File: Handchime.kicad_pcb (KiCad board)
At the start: 4 copper layers, 40.6 x 20.2 mm, 23 parts, among them J1 USB_C_Receptacle_USB2.0_16P, J2 Pins, J3 SWD, SW0 BOOT, SW1 Row 0, Col 0, SW2 Row 0, Col 1, U1 STM32C071GBUx, U2 PRTR5V0U2X, U3 XC6206P332MR-G

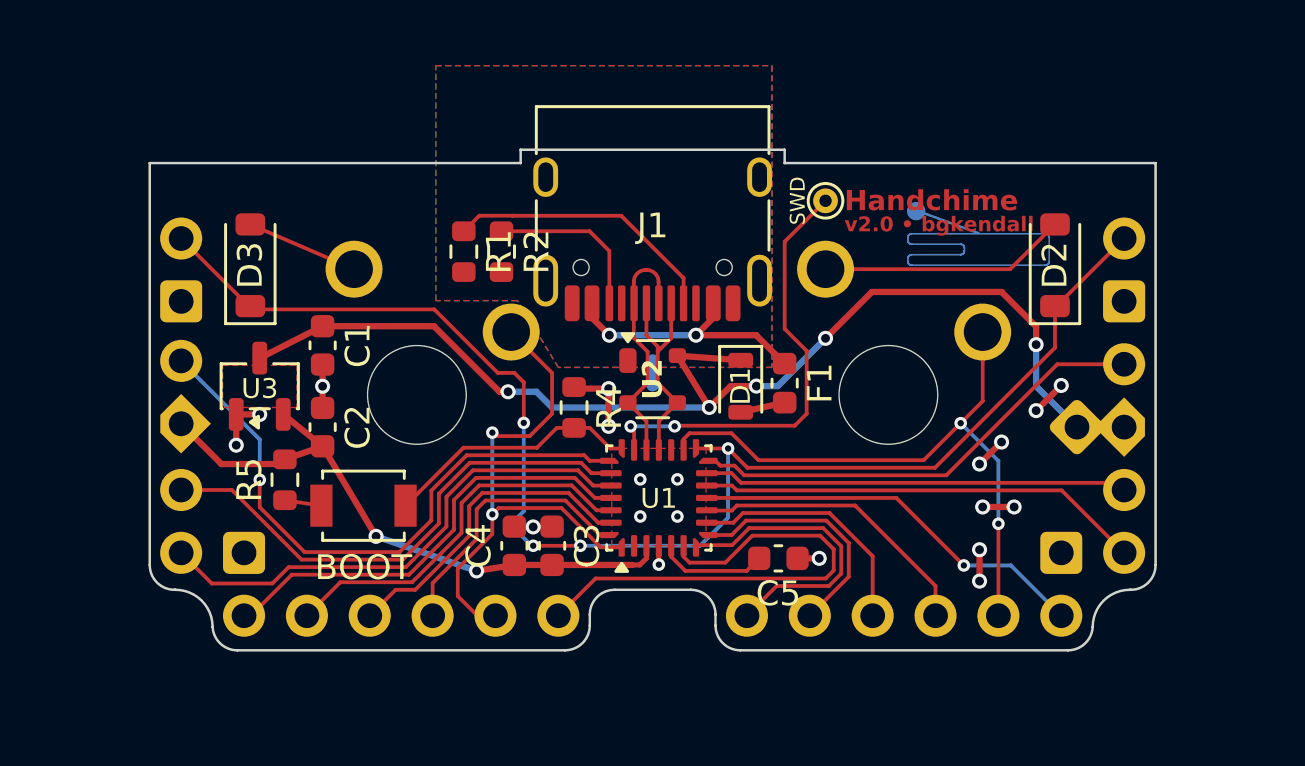
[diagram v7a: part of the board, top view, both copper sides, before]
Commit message: Add 2-hole SWD access point
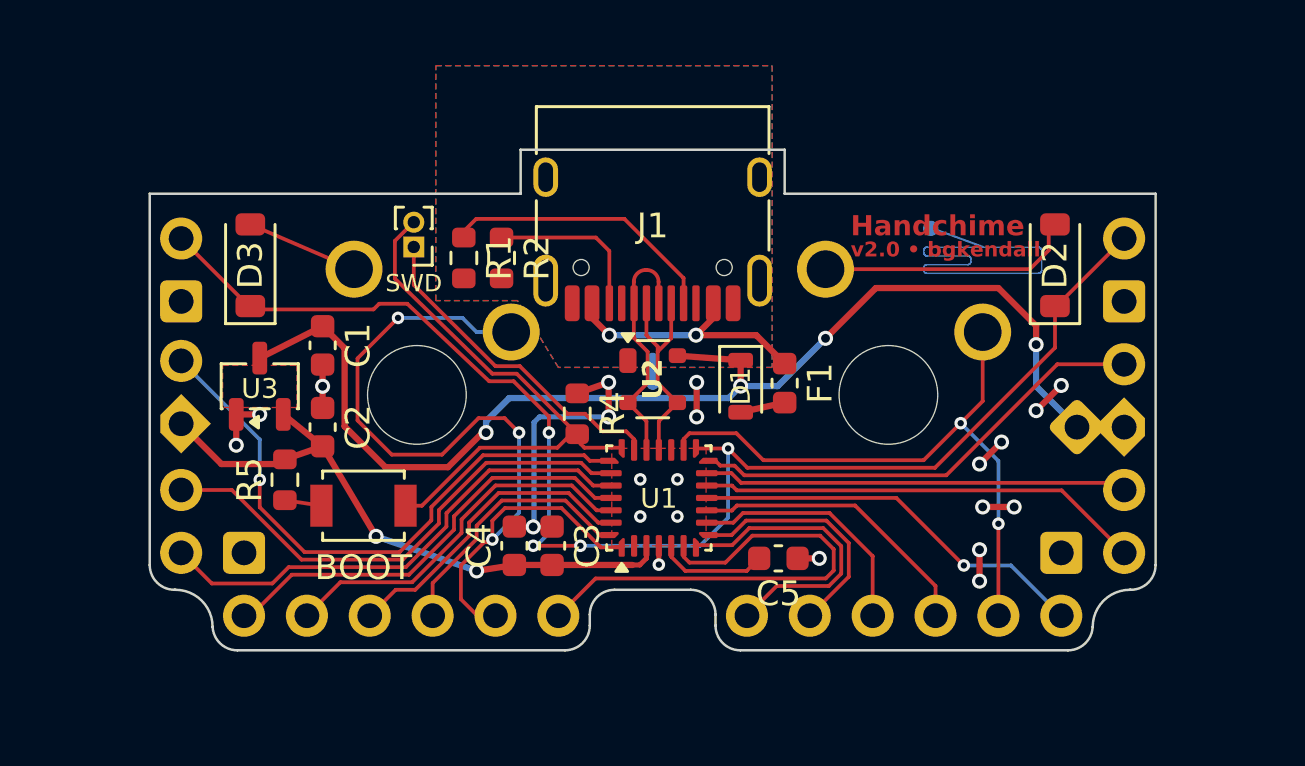
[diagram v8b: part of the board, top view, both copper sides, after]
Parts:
- J3: footprint TestPoint:TestPoint_THTPad_D1.0mm_Drill0.5mm -> Connector_PinHeader_1.00mm:PinHeader_1x02_P1.00mm_Vertical
- moved J3 16.7 mm to (142.7, 44.8), turned to 180 degrees
- moved R4 0.28 mm to (149.4, 51.6)
- moved R1 0.25 mm to (144.8, 45.3)
- moved R2 0.25 mm to (146.3, 45.3)
- moved NT1 0.06 mm to (152.4, 49.8)
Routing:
- net BOOT0/SWCLK: track 10.4 -> 23.0 mm
- net C1: track 21.9 -> 33.9 mm, vias 2 -> 3
- net GND: track 15.3 -> 23.8 mm, vias 20 -> 22
- net SWDIO: track 18.1 -> 13.2 mm, vias 2 -> 0
- net VCC: track 45.3 -> 48.4 mm, vias 5 -> 4
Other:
- outline, holes or cut-outs redrawn
